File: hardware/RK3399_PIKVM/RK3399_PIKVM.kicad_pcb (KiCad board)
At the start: 2 copper layers, 8 parts

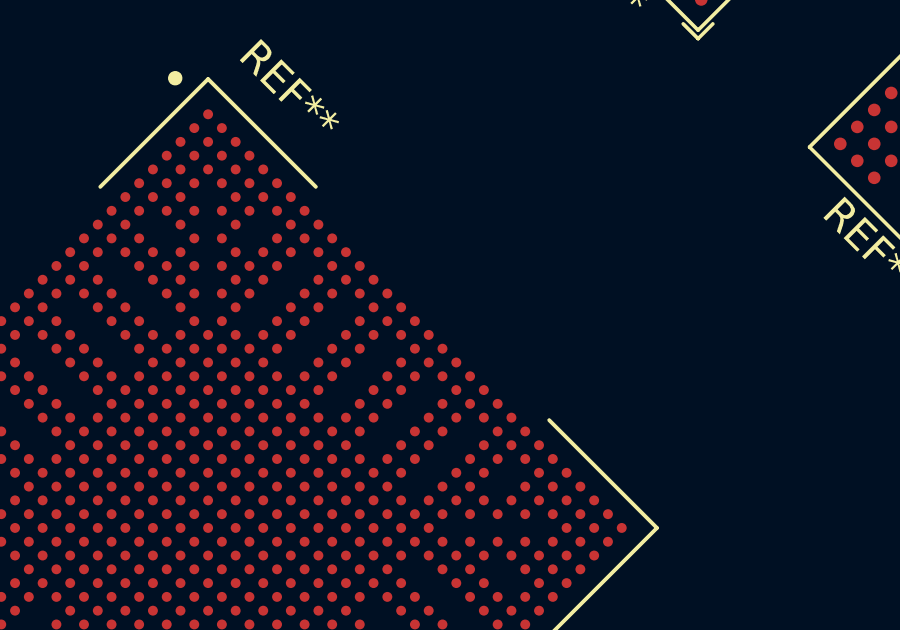
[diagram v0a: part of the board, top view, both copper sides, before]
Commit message: Did some fan-out layout test, add some basic PCB layout rules.
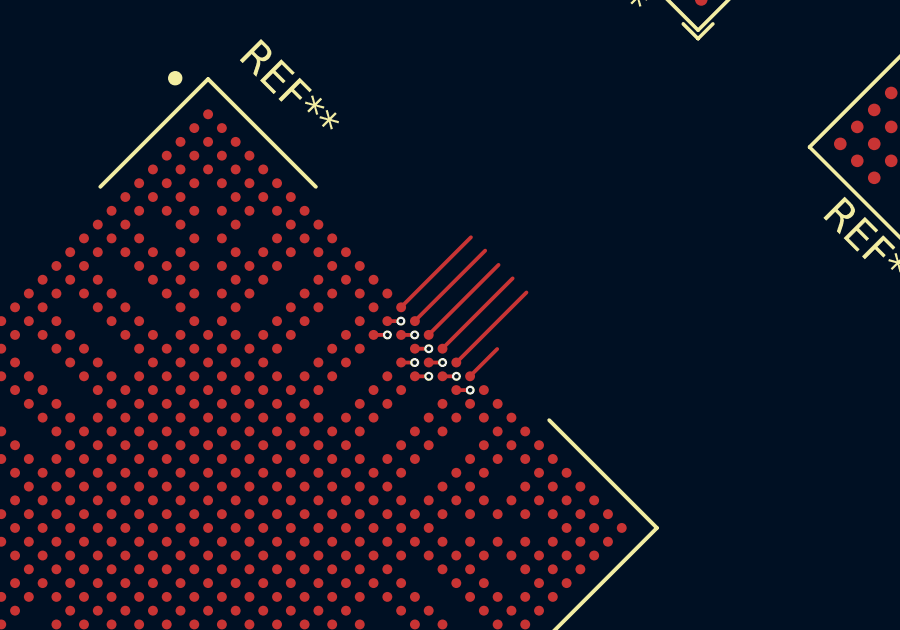
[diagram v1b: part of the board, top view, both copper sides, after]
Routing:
- net (no net): track 0.00 -> 34.5 mm, vias 0 -> 9
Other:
- copper layers 2 -> 6
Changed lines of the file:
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@@
   (layers
     (0 "F.Cu" signal)
+    (1 "In1.Cu" signal)
+    (2 "In2.Cu" signal)
+    (3 "In3.Cu" signal)
+    (4 "In4.Cu" signal)
     (31 "B.Cu" signal)
     (32 "B.Adhes" user "B.Adhesive")
@@
       (layer "F.Mask" (type "Top Solder Mask") (thickness 0.01))
       (layer "F.Cu" (type "copper") (thickness 0.035))
-      (layer "dielectric 1" (type "core") (thickness 1.51) (material "FR4") (epsilon_r 4.5) (loss_tangent 0.02))
+      (layer "dielectric 1" (type "prepreg") (thickness 0.1) (material "FR4") (epsilon_r 4.5) (loss_tangent 0.02))
+      (layer "In1.Cu" (type "copper") (thickness 0.035))
+      (layer "dielectric 2" (type "core") (thickness 0.535) (material "FR4") (epsilon_r 4.5) (loss_tangent 0.02))
+      (layer "In2.Cu" (type "copper") (thickness 0.035))
+      (layer "dielectric 3" (type "prepreg") (thickness 0.1) (material "FR4") (epsilon_r 4.5) (loss_tangent 0.02))
+      (layer "In3.Cu" (type "copper") (thickness 0.035))
+      (layer "dielectric 4" (type "core") (thickness 0.535) (material "FR4") (epsilon_r 4.5) (loss_tangent 0.02))
+      (layer "In4.Cu" (type "copper") (thickness 0.035))
+      (layer "dielectric 5" (type "prepreg") (thickness 0.1) (material "FR4") (epsilon_r 4.5) (loss_tangent 0.02))
       (layer "B.Cu" (type "copper") (thickness 0.035))
       (layer "B.Mask" (type "Bottom Solder Mask") (thickness 0.01))
@@
     (pad "69" smd rect (at 0 0 270) (size 5.63 5.63) (layers "F.Cu" "F.Mask"))
   )
+  (segment (start 142.968283 92.238283) (end 142.97 92.24) (width 0.1524) (layer "F.Cu") (net 0))
+  (segment (start 142.981262 91.78) (end 143.44 91.78) (width 0.127) (layer "F.Cu") (net 0))
+  (segment (start 143.901262 92.7) (end 144.36 92.7) (width 0.127) (layer "F.Cu") (net 0))
+  (segment (start 143.441262 92.24) (end 143.9 92.24) (width 0.127) (layer "F.Cu") (net 0))
+  (segment (start 144.361262 93.16) (end 144.82 93.16) (width 0.127) (layer "F.Cu") (net 0))
+  (segment (start 142.511262 92.24) (end 142.97 92.24) (width 0.127) (layer "F.Cu") (net 0))
+  (segment (start 142.511262 91.32) (end 142.97 91.32) (width 0.127) (layer "F.Cu") (net 0))
+  (segment (start 142.051262 90.86) (end 142.51 90.86) (width 0.127) (layer "F.Cu") (net 0))
+  (segment (start 142.989628 90.840372) (end 145.32 88.51) (width 0.127) (layer "F.Cu") (net 0))
+  (segment (start 143.434814 91.315186) (end 145.765186 88.984814) (width 0.127) (layer "F.Cu") (net 0))
+  (segment (start 144.364814 92.235186) (end 146.695186 89.904814) (width 0.127) (layer "F.Cu") (net 0))
+  (segment (start 142.519628 90.400372) (end 142.519628 90.390372) (width 0.127) (layer "F.Cu") (net 0))
+  (segment (start 143.904814 91.765186) (end 146.235186 89.434814) (width 0.127) (layer "F.Cu") (net 0))
+  (segment (start 142.981262 92.7) (end 143.44 92.7) (width 0.127) (layer "F.Cu") (net 0))
+  (segment (start 142.514814 90.395186) (end 144.845186 88.064814) (width 0.127) (layer "F.Cu") (net 0))
+  (segment (start 143.437903 92.697903) (end 143.44 92.7) (width 0.1524) (layer "F.Cu") (net 0))
+  (segment (start 141.598955 91.319044) (end 142.057693 91.319044) (width 0.127) (layer "F.Cu") (net 0))
+  (segment (start 144.819257 92.690744) (end 145.72 91.79) (width 0.127) (layer "F.Cu") (net 0))
+  (segment (start 142.989628 90.860372) (end 142.989628 90.840372) (width 0.127) (layer "F.Cu") (net 0))
+  (via (at 142.97 92.24) (size 0.3) (drill 0.15) (layers "F.Cu" "B.Cu") (net 0))
+  (via (at 143.44 91.78) (size 0.3) (drill 0.15) (layers "F.Cu" "B.Cu") (net 0))
+  (via (at 143.44 92.7) (size 0.3) (drill 0.15) (layers "F.Cu" "B.Cu") (net 0))
+  (via (at 142.97 91.32) (size 0.3) (drill 0.15) (layers "F.Cu" "B.Cu") (net 0))
+  (via (at 143.9 92.24) (size 0.3) (drill 0.15) (layers "F.Cu" "B.Cu") (net 0))
+  (via (at 142.06 91.32) (size 0.3) (drill 0.15) (layers "F.Cu" "B.Cu") (net 0))
+  (via (at 144.36 92.7) (size 0.3) (drill 0.15) (layers "F.Cu" "B.Cu") (net 0))
+  (via (at 144.82 93.16) (size 0.3) (drill 0.15) (layers "F.Cu" "B.Cu") (net 0))
+  (via (at 142.510649 90.859425) (size 0.3) (drill 0.15) (layers "F.Cu" "B.Cu") (net 0))
+  (arc (start 143.436775 91.778664) (mid 143.43852 91.779011) (end 143.44 91.78) (width 0.1524) (layer "F.Cu") (net 0))
+  (arc (start 142.058574 89.940186) (mid 142.063046 89.939297) (end 142.066837 89.936764) (width 0.1778) (layer "F.Cu") (net 0))
+  (arc (start 144.816291 92.697903) (mid 144.817062 92.694028) (end 144.819257 92.690744) (width 0.127) (layer "F.Cu") (net 0))
+  (arc (start 144.354938 92.697903) (mid 144.357677 92.698448) (end 144.36 92.7) (width 0.1524) (layer "F.Cu") (net 0))
+  (arc (start 142.967693 91.319044) (mid 142.968941 91.319293) (end 142.97 91.32) (width 0.1524) (layer "F.Cu") (net 0))
+  (arc (start 142.057693 91.319044) (mid 142.058941 91.319293) (end 142.06 91.32) (width 0.127) (layer "F.Cu") (net 0))
+  (arc (start 143.895855 92.238283) (mid 143.898098 92.238729) (end 143.9 92.24) (width 0.1524) (layer "F.Cu") (net 0))
+  (arc (start 144.814018 93.157522) (mid 144.817255 93.158165) (end 144.82 93.16) (width 0.1524) (layer "F.Cu") (net 0))
+  (arc (start 142.058574 90.859425) (mid 142.062589 90.856743) (end 142.067325 90.8558) (width 0.1778) (layer "F.Cu") (net 0))
+  (segment (start 144.36 92.7) (end 145.53 91.53) (width 0.127) (layer "In2.Cu") (net 0))
+  (segment (start 143.9 92.24) (end 145.09 91.05) (width 0.127) (layer "In2.Cu") (net 0))
+  (segment (start 142.97 91.32) (end 144.12 90.17) (width 0.127) (layer "In2.Cu") (net 0))
+  (segment (start 142.515 90.855) (end 143.665 89.705) (width 0.127) (layer "In2.Cu") (net 0))
+  (segment (start 143.445 91.775) (end 144.595 90.625) (width 0.127) (layer "In2.Cu") (net 0))
+  (segment (start 143.446274 92.7) (end 143.67 92.7) (width 0.127) (layer "In4.Cu") (net 0))
+  (segment (start 144.056274 92.54) (end 144.606274 91.99) (width 0.127) (layer "In4.Cu") (net 0))
+  (segment (start 142.06 91.32) (end 142.283726 91.32) (width 0.127) (layer "In4.Cu") (net 0))
+  (segment (start 143.586274 92.08) (end 144.136274 91.53) (width 0.127) (layer "In4.Cu") (net 0))
+  (segment (start 142.976274 92.24) (end 143.2 92.24) (width 0.127) (layer "In4.Cu") (net 0))
+  (segment (start 142.67 91.16) (end 143.22 90.61) (width 0.127) (layer "In4.Cu") (net 0))
+  (arc (start 143.67 92.7) (mid 143.87905 92.658418) (end 144.056274 92.54) (width 0.127) (layer "In4.Cu") (net 0))
+  (arc (start 143.2 92.24) (mid 143.40905 92.198418) (end 143.586274 92.08) (width 0.127) (layer "In4.Cu") (net 0))
+  (arc (start 142.283726 91.32) (mid 142.492776 91.278418) (end 142.67 91.16) (width 0.127) (layer "In4.Cu") (net 0))
 )
